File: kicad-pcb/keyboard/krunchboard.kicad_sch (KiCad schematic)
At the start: 198 parts, among them J1 Conn_01x04_Pin, J2 Conn_01x04_Pin, SW1 SW_Push_45deg, SW10 SW_Push_45deg, SW11 SW_Push_45deg, SW12 SW_Push_45deg, SW13 SW_Push_45deg, SW14 SW_Push_45deg, SW15 SW_Push_45deg, SW16 SW_Push_45deg, SW17 SW_Push_45deg, SW18 SW_Push_45deg, SW19 SW_Push_45deg, SW2 SW_Push_45deg, SW20 SW_Push_45deg, SW21 SW_Push_45deg, SW22 SW_Push_45deg, SW23 SW_Push_45deg, SW24 SW_Push_45deg, SW25 SW_Push_45deg, SW26 SW_Push_45deg, SW27 SW_Push_45deg, SW28 SW_Push_45deg, SW29 SW_Push_45deg, SW3 SW_Push_45deg, SW30 SW_Push_45deg, SW31 SW_Push_45deg, SW32 SW_Push_45deg, SW33 SW_Push_45deg, SW34 SW_Push_45deg, SW35 SW_Push_45deg, SW36 SW_Push_45deg, SW37 SW_Push_45deg, SW38 SW_Push_45deg, SW39 SW_Push_45deg, SW4 SW_Push_45deg, SW40 SW_Push_45deg, SW41 SW_Push_45deg, SW42 SW_Push_45deg, SW43 SW_Push_45deg, SW44 SW_Push_45deg, SW45 SW_Push_45deg, SW46 SW_Push_45deg, SW47 SW_Push_45deg, SW48 SW_Push_45deg, SW49 SW_Push_45deg, SW5 SW_Push_45deg, SW50 SW_Push_45deg, SW51 SW_Push_45deg, SW52 SW_Push_45deg, SW53 SW_Push_45deg, SW54 SW_Push_45deg, SW55 SW_Push_45deg, SW56 SW_Push_45deg, SW57 SW_Push_45deg, SW58 SW_Push_45deg, SW59 SW_Push_45deg, SW6 SW_Push_45deg, SW60 SW_Push_45deg, SW61 SW_Push_45deg, SW62 SW_Push_45deg, SW63 SW_Push_45deg, SW64 SW_Push_45deg, SW65 SW_Push_45deg, SW66 SW_Push_45deg, SW67 SW_Push_45deg, SW68 SW_Push_45deg, SW69 SW_Push_45deg, SW7 SW_Push_45deg, SW70 SW_Push_45deg, SW71 SW_Push_45deg, SW72 SW_Push_45deg, SW73 SW_Push_45deg, SW74 SW_Push_45deg, SW75 SW_Push_45deg, SW76 SW_Push_45deg, SW77 SW_Push_45deg, SW78 SW_Push_45deg, SW79 SW_Push_45deg, SW8 SW_Push_45deg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

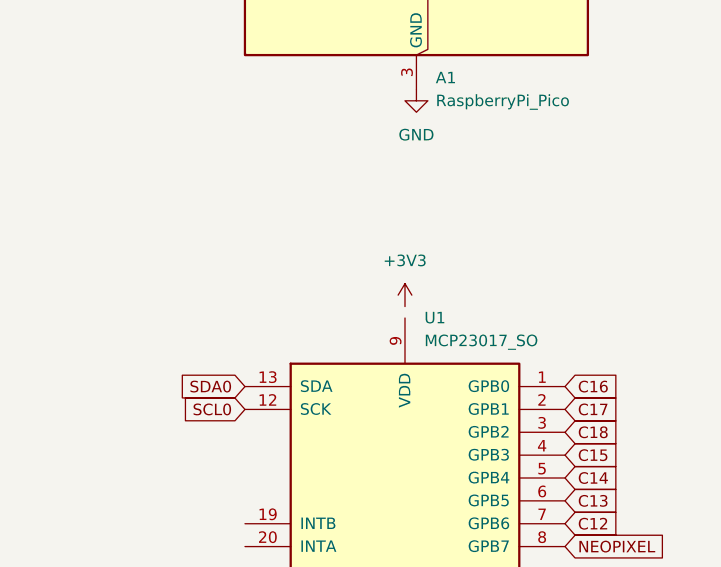
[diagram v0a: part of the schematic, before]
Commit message: switched mounting styles, updated pcb, plate, and case
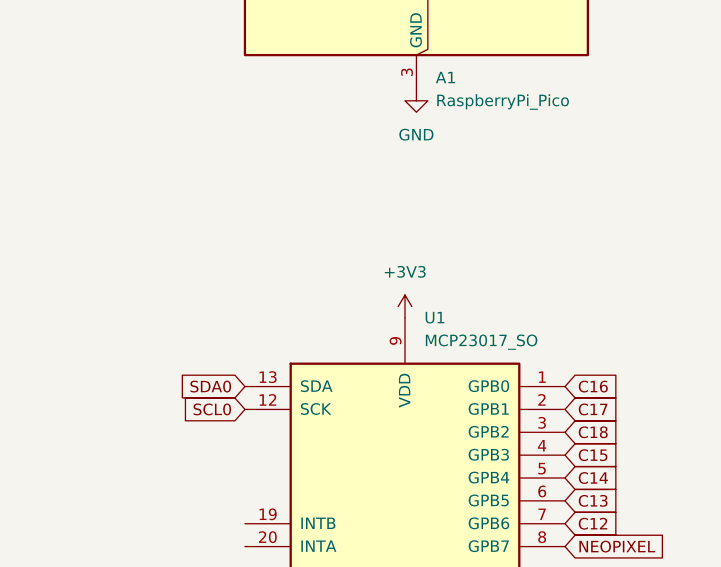
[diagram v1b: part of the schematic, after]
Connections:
- net +3V3: now also U1.9 (VDD)

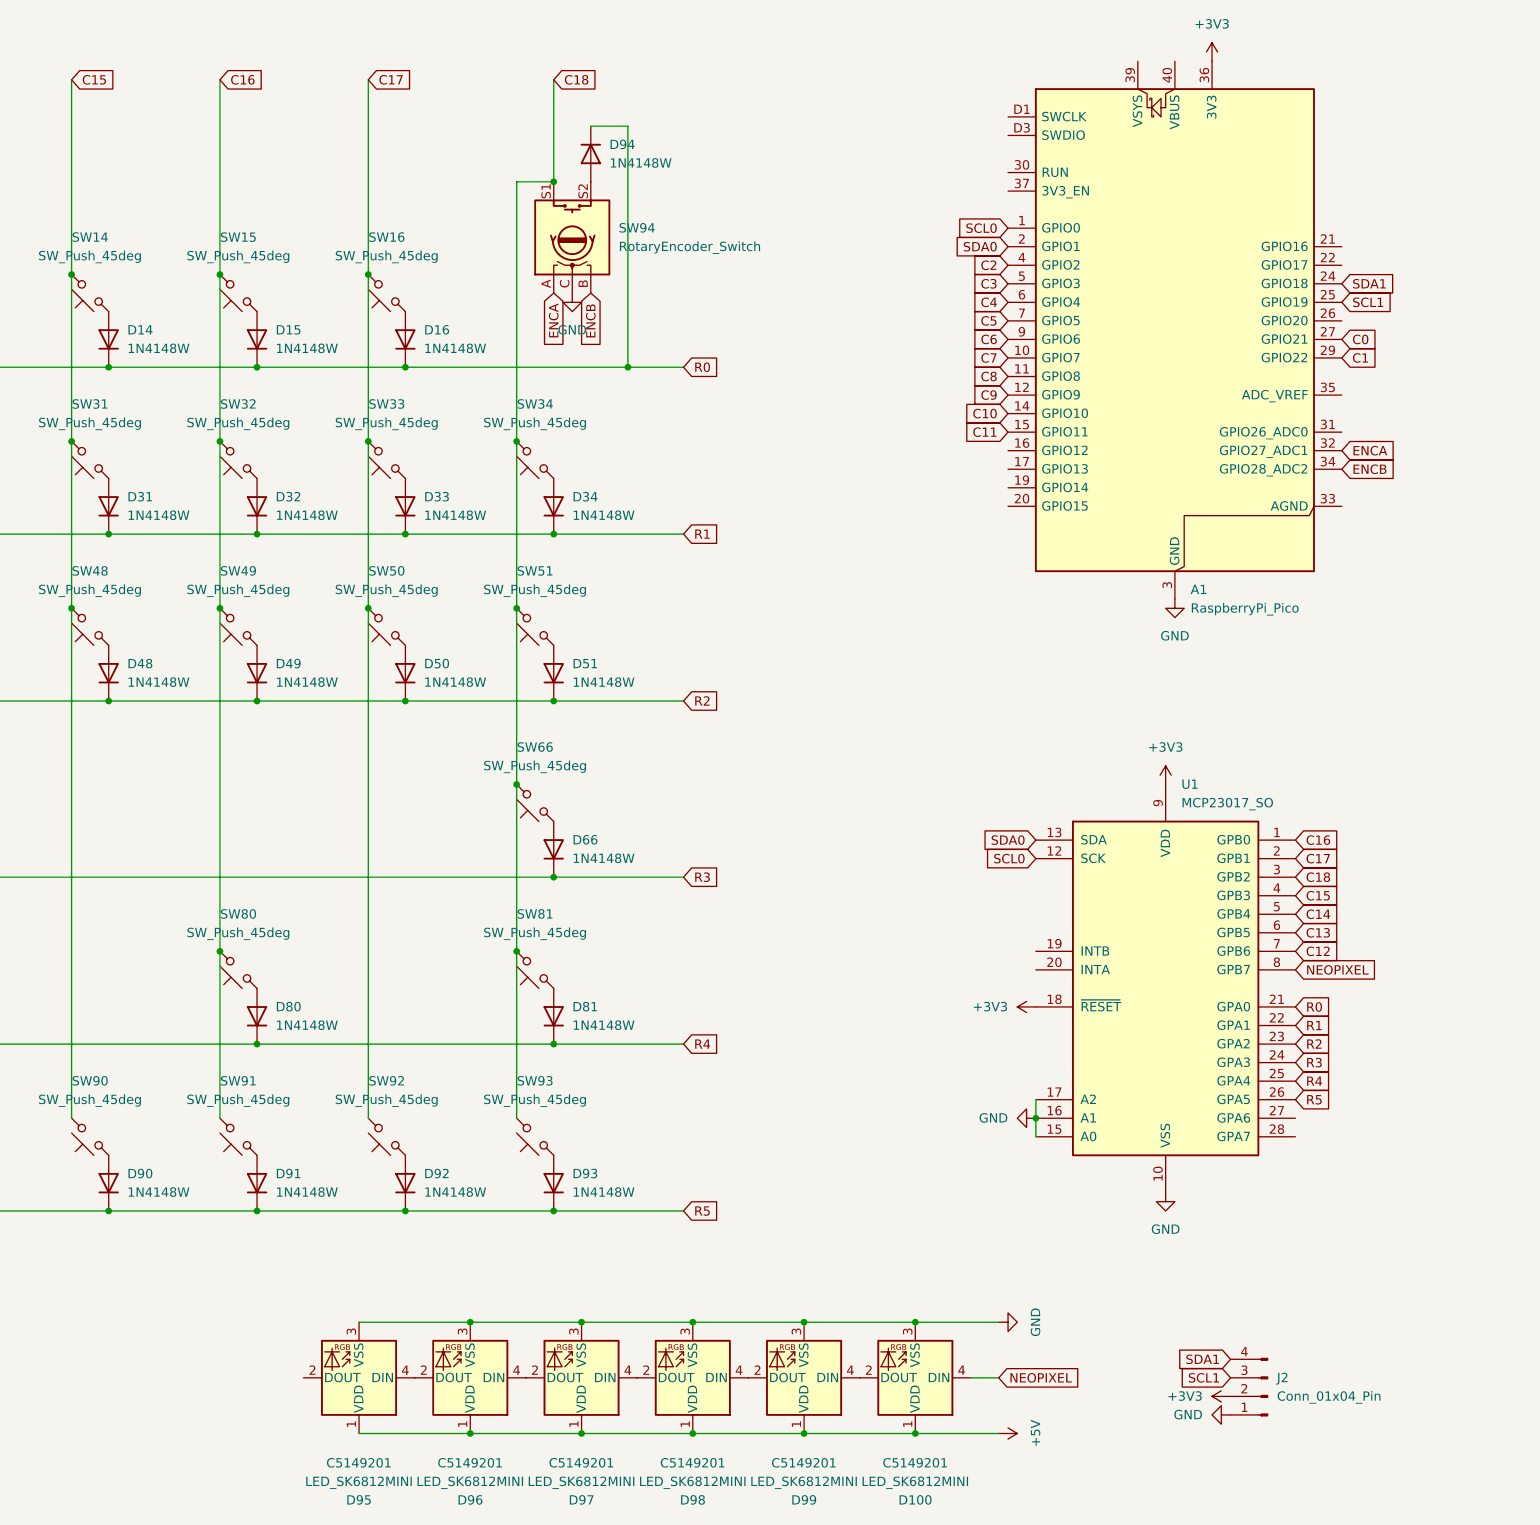
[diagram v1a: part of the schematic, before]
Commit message: updated pcb - switched oled socket from smd to tht, added hole for tht socket in case, adjusted pcb vias and silkscreen, added testpoints to pcb
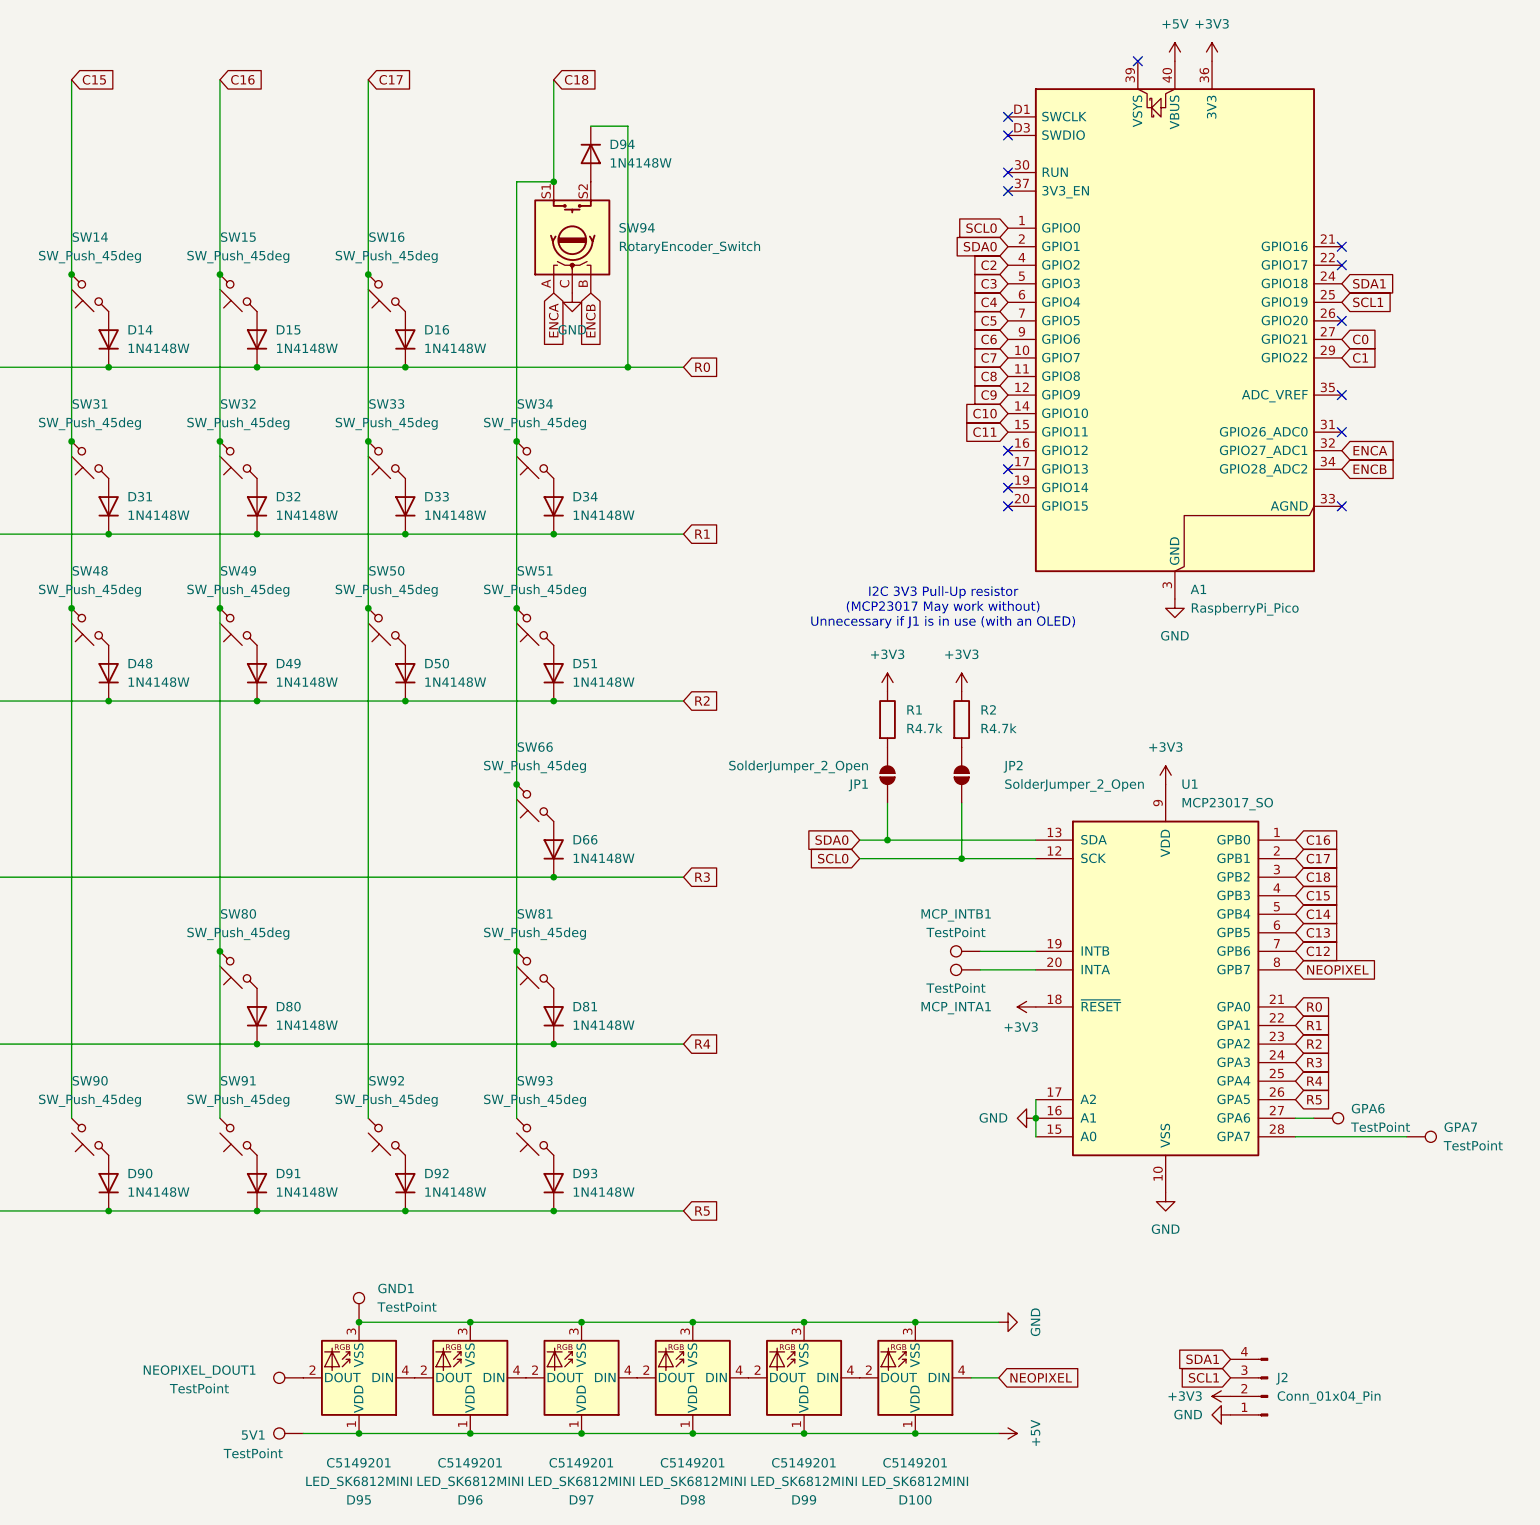
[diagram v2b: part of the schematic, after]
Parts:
- added 5V1, GND1, GPA6, GPA7, MCP_INTA1, MCP_INTB1, NEOPIXEL_DOUT1: TestPoint, TestPoint:TestPoint_Pad_D2.5mm, symbol Connector:TestPoint
- added JP1, JP2: SolderJumper_2_Open, Jumper:SolderJumper-2_P1.3mm_Open_TrianglePad1.0x1.5mm, symbol Jumper:SolderJumper_2_Open
- added R1, R2: R4.7k, Resistor_SMD:R_0805_2012Metric_Pad1.20x1.40mm_HandSolder, symbol Device:R
- J1, J2: footprint Connector_PinSocket_2.54mm:PinSocket_1x04_P2.54mm_Vertical_SMD_Pin1Left -> Connector_PinSocket_2.54mm:PinSocket_1x04_P2.54mm_Vertical
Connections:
- net +3V3: now also R1.1, R2.1
- net +5V: now also A1.40 (VBUS), 5V1.1
- net GND: now also GND1.1
- net SCL0: now also JP2.2 (B)
- net SDA0: now also JP1.2 (B)
- net at D95.2 (DOUT): now also NEOPIXEL_DOUT1.1
- net at U1.19 (INTB): now also MCP_INTB1.1
- net at U1.20 (INTA): now also MCP_INTA1.1
- net at U1.27 (GPA6): now also GPA6.1
- net at U1.28 (GPA7): now also GPA7.1
- new net: JP2.1 (A), R2.2
- new net: JP1.1 (A), R1.2
- no-connect marks 0 -> 15
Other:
- note added: "I2C 3V3 Pull-Up resistor (MCP23017 May work without) Unnecessary if J1 is in use (with an OLED)"
